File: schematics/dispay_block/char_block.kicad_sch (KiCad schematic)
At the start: 16 parts

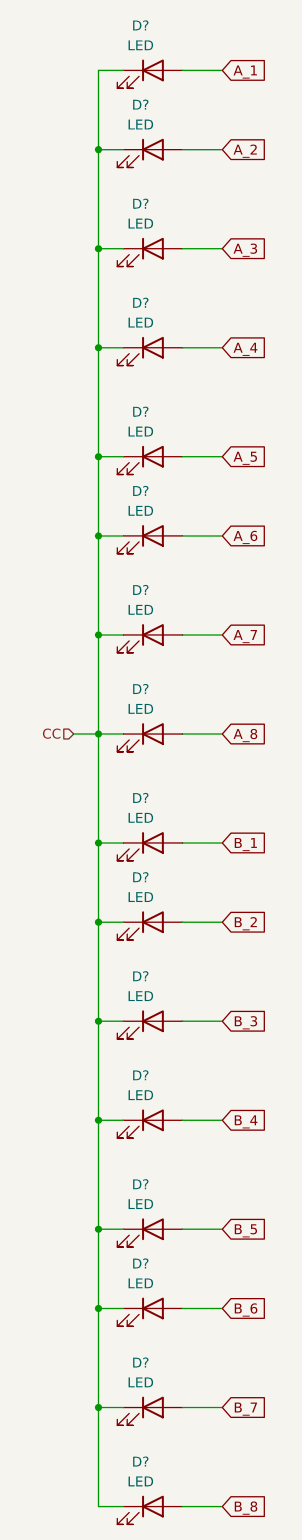
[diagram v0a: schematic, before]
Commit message: hw: annotate schematics and add capacitor footprints
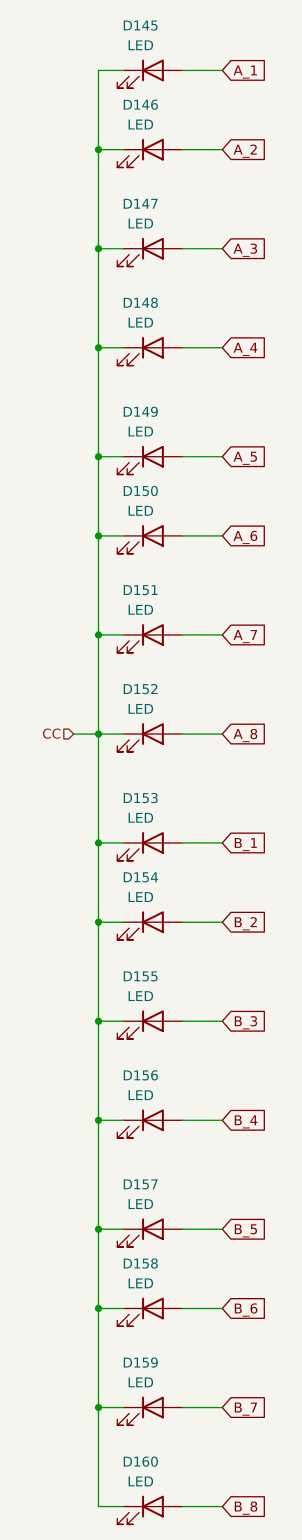
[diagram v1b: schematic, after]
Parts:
- gave numbers to parts that had none: 16

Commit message: hw: add display segment schematic and PCB v1
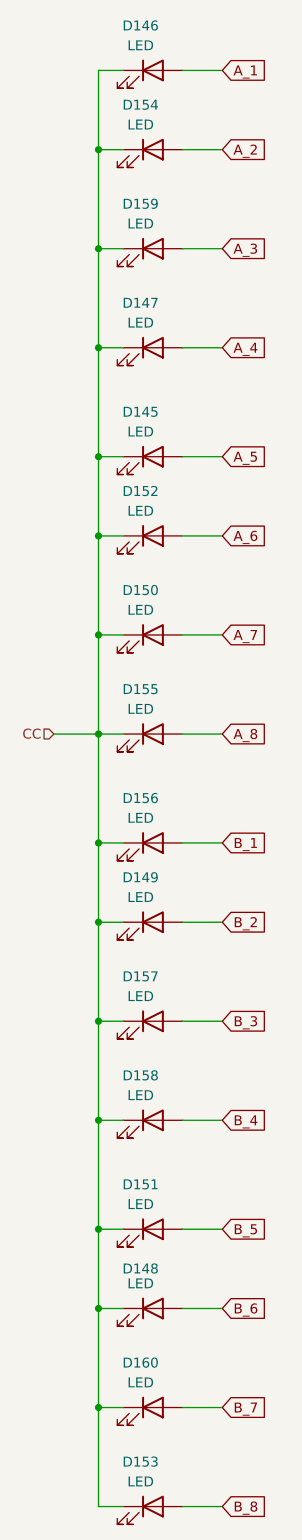
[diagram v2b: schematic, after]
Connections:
- net A_1: now also D146.2 (A); no longer D145.2 (A)
- net A_2: now also D154.2 (A); no longer D146.2 (A)
- net A_3: now also D159.2 (A); no longer D147.2 (A)
- net A_4: now also D147.2 (A); no longer D148.2 (A)
- net A_5: now also D145.2 (A); no longer D149.2 (A)
- net A_6: now also D152.2 (A); no longer D150.2 (A)
- net A_7: now also D150.2 (A); no longer D151.2 (A)
- net A_8: now also D155.2 (A); no longer D152.2 (A)
- net B_1: now also D156.2 (A); no longer D153.2 (A)
- net B_2: now also D149.2 (A); no longer D154.2 (A)
- net B_3: now also D157.2 (A); no longer D155.2 (A)
- net B_4: now also D158.2 (A); no longer D156.2 (A)
- net B_5: now also D151.2 (A); no longer D157.2 (A)
- net B_6: now also D148.2 (A); no longer D158.2 (A)
- net B_7: now also D160.2 (A); no longer D159.2 (A)
- net B_8: now also D153.2 (A); no longer D160.2 (A)
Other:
- company: (none) -> Author: Kacper Jelonek
- moved on the sheet: D145, D146, D147, D148, D149, D150, D151, D152, D153, D154, D155, D156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

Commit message: hw: revise display design and fix wrong footprint
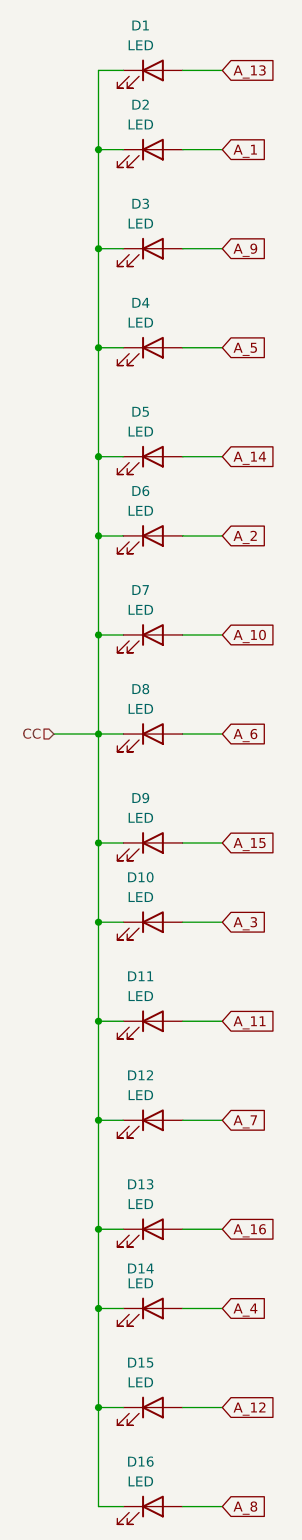
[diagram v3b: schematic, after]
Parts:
- D1: renamed from D146; footprint LED_SMD:LED_0201_0603Metric -> LED_SMD:LED_0603_1608Metric
- D10: renamed from D149; footprint LED_SMD:LED_0201_0603Metric -> LED_SMD:LED_0603_1608Metric
- D11: renamed from D157; footprint LED_SMD:LED_0201_0603Metric -> LED_SMD:LED_0603_1608Metric
- D12: renamed from D158; footprint LED_SMD:LED_0201_0603Metric -> LED_SMD:LED_0603_1608Metric
- D13: renamed from D151; footprint LED_SMD:LED_0201_0603Metric -> LED_SMD:LED_0603_1608Metric
- D14: renamed from D148; footprint LED_SMD:LED_0201_0603Metric -> LED_SMD:LED_0603_1608Metric
- D15: renamed from D160; footprint LED_SMD:LED_0201_0603Metric -> LED_SMD:LED_0603_1608Metric
- D16: renamed from D153; footprint LED_SMD:LED_0201_0603Metric -> LED_SMD:LED_0603_1608Metric
- D2: renamed from D154; footprint LED_SMD:LED_0201_0603Metric -> LED_SMD:LED_0603_1608Metric
- D3: renamed from D159; footprint LED_SMD:LED_0201_0603Metric -> LED_SMD:LED_0603_1608Metric
- D4: renamed from D147; footprint LED_SMD:LED_0201_0603Metric -> LED_SMD:LED_0603_1608Metric
- D5: renamed from D145; footprint LED_SMD:LED_0201_0603Metric -> LED_SMD:LED_0603_1608Metric
- D6: renamed from D152; footprint LED_SMD:LED_0201_0603Metric -> LED_SMD:LED_0603_1608Metric
- D7: renamed from D150; footprint LED_SMD:LED_0201_0603Metric -> LED_SMD:LED_0603_1608Metric
- D8: renamed from D155; footprint LED_SMD:LED_0201_0603Metric -> LED_SMD:LED_0603_1608Metric
- D9: renamed from D156; footprint LED_SMD:LED_0201_0603Metric -> LED_SMD:LED_0603_1608Metric
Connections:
- net B_2 is gone; now on net A_3: D10.2 (A)
- net B_4 is gone; now on net A_7: D12.2 (A)
- net B_6 is gone; now on net A_4: D14.2 (A)
- net B_8 is gone; now on net A_8: D16.2 (A)
- net A_1: now also D2.2 (A); no longer D1.2 (A)
- net A_2: now also D6.2 (A); no longer D2.2 (A)
- net A_3: no longer D3.2 (A)
- net A_4: no longer D4.2 (A)
- net A_5: now also D4.2 (A); no longer D5.2 (A)
- net A_6: now also D8.2 (A); no longer D6.2 (A)
- net A_7: no longer D7.2 (A)
- net A_8: no longer D8.2 (A)
- net B_1 renamed A_15
- net B_3 renamed A_11
- net B_5 renamed A_16
- net B_7 renamed A_12
- new net A_10: D7.2 (A)
- new net A_13: D1.2 (A)
- new net A_14: D5.2 (A)
- new net A_9: D3.2 (A)
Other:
- title: Char Block -> CHAR_BLOCK
